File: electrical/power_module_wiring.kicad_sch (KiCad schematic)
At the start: 8 parts, among them J1 Power, J12 Conn_01x02_Pin, J13 11156, J14 Conn_01x02_Socket, J15 11155, J3 Bulb, J3 Ground

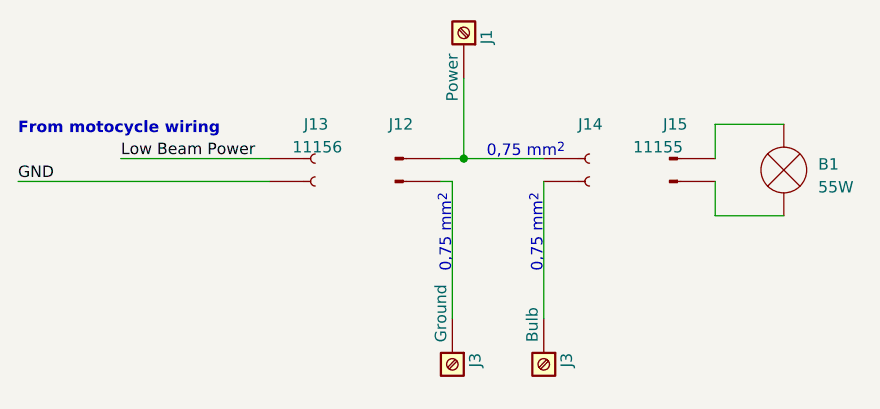
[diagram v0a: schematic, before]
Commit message: Electrical diagram refactor
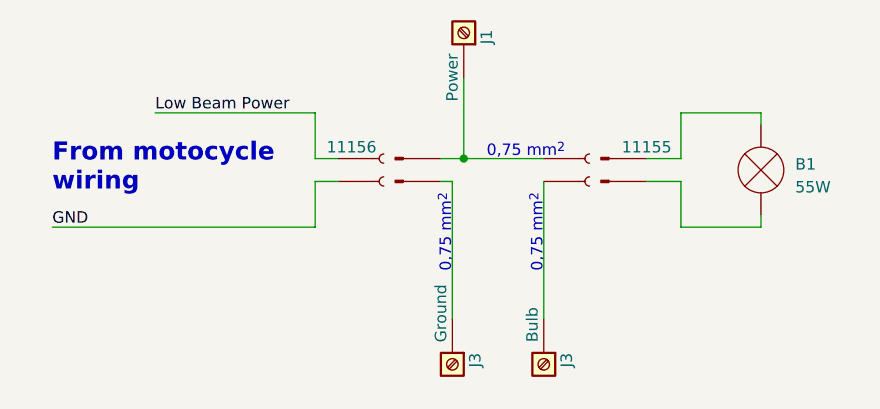
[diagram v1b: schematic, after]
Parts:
- renumbered J13 to J12, J12 to J13
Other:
- moved on the sheet: B1
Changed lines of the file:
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@@
   (junction (at 80.01 67.31) (diameter 0) (color 0 0 0 0)
   )
+  (wire (pts (xy 63.5 74.93) (xy 63.5 69.85))
+    (stroke (width 0) (type default))
+  )
+  (wire (pts (xy 113.03 74.93) (xy 113.03 73.66))
+    (stroke (width 0) (type default))
+  )
+  (wire (pts (xy 63.5 62.23) (xy 63.5 67.31))
+    (stroke (width 0) (type default))
+  )
   (wire (pts (xy 78.74 69.85) (xy 77.47 69.85))
     (stroke (width 0) (type default))
@@
     (stroke (width 0) (type default))
   )
-  (wire (pts (xy 41.91 67.31) (xy 58.42 67.31))
+  (wire (pts (xy 104.14 67.31) (xy 100.33 67.31))
+    (stroke (width 0) (type default))
+  )
+  (wire (pts (xy 45.72 62.23) (xy 63.5 62.23))
+    (stroke (width 0) (type default))
+  )
+  (wire (pts (xy 63.5 67.31) (xy 66.04 67.31))
     (stroke (width 0) (type default))
   )
@@
     (stroke (width 0) (type default))
   )
-  (wire (pts (xy 107.95 67.31) (xy 107.95 63.5))
-    (stroke (width 0) (type default))
-  )
-  (wire (pts (xy 107.95 63.5) (xy 115.57 63.5))
+  (wire (pts (xy 63.5 69.85) (xy 66.04 69.85))
+    (stroke (width 0) (type default))
+  )
+  (wire (pts (xy 113.03 62.23) (xy 113.03 63.5))
+    (stroke (width 0) (type default))
+  )
+  (wire (pts (xy 104.14 67.31) (xy 104.14 62.23))
+    (stroke (width 0) (type default))
+  )
+  (wire (pts (xy 104.14 62.23) (xy 113.03 62.23))
     (stroke (width 0) (type default))
   )
@@
     (stroke (width 0) (type default))
   )
-  (wire (pts (xy 30.48 69.85) (xy 58.42 69.85))
-    (stroke (width 0) (type default))
-  )
-  (wire (pts (xy 107.95 69.85) (xy 107.95 73.66))
-    (stroke (width 0) (type default))
-  )
-  (wire (pts (xy 107.95 73.66) (xy 115.57 73.66))
-    (stroke (width 0) (type default))
-  )
-  (text "From motocycle wiring" (at 30.48 64.77 0)
-    (effects (font (size 1.27 1.27) (thickness 0.254) bold) (justify left bottom))
+  (wire (pts (xy 104.14 69.85) (xy 100.33 69.85))
+    (stroke (width 0) (type default))
+  )
+  (wire (pts (xy 34.29 74.93) (xy 63.5 74.93))
+    (stroke (width 0) (type default))
+  )
+  (wire (pts (xy 104.14 69.85) (xy 104.14 74.93))
+    (stroke (width 0) (type default))
+  )
+  (wire (pts (xy 104.14 74.93) (xy 113.03 74.93))
+    (stroke (width 0) (type default))
+  )
+  (text "From motocycle\nwiring" (at 34.29 71.12 0)
+    (effects (font (size 2 2) (thickness 0.254) bold) (justify left bottom))
   )
   (text "0,75 mm^{2}" (at 82.55 67.31 0)
@@
     (effects (font (size 1.27 1.27)) (justify left bottom))
   )
-  (label "Low Beam Power" (at 41.91 67.31 0) (fields_autoplaced)
-    (effects (font (size 1.27 1.27)) (justify left bottom))
-    (property "Color" "B/Bl" (at 41.91 68.58 0) (show_name)
+  (label "Low Beam Power" (at 45.72 62.23 0) (fields_autoplaced)
+    (effects (font (size 1.27 1.27)) (justify left bottom))
+    (property "Color" "B/Bl" (at 45.72 63.5 0) (show_name)
       (effects (font (size 1.27 1.27) italic) (justify left))
     )
   )
-  (label "GND" (at 30.48 69.85 0) (fields_autoplaced)
-    (effects (font (size 1.27 1.27)) (justify left bottom))
-    (property "Color" "B/W" (at 30.48 71.12 0) (show_name)
+  (label "GND" (at 34.29 74.93 0) (fields_autoplaced)
+    (effects (font (size 1.27 1.27)) (justify left bottom))
+    (property "Color" "B/W" (at 34.29 76.2 0) (show_name)
       (effects (font (size 1.27 1.27) italic) (justify left))
     )
@@
     )
   )
-  (symbol (lib_name "Conn_01x02_Pin_1") (lib_id "Connector:Conn_01x02_Pin") (at 102.87 67.31 0) (unit 1)
-    (in_bom yes) (on_board yes) (dnp no)
-    (property "Reference" "J15" (at 103.505 63.5 0)
+  (symbol (lib_name "Conn_01x02_Pin_1") (lib_id "Connector:Conn_01x02_Pin") (at 95.25 67.31 0) (unit 1)
+    (in_bom yes) (on_board yes) (dnp no)
+    (property "Reference" "J15" (at 95.885 63.5 0)
+      (effects (font (size 1.27 1.27)) hide)
+    )
+    (property "Value" "11155" (at 100.33 66.04 0)
       (effects (font (size 1.27 1.27)))
     )
-    (property "Value" "11155" (at 101.6 66.04 0)
-      (effects (font (size 1.27 1.27)))
-    )
-    (property "Footprint" "" (at 102.87 67.31 0)
-      (effects (font (size 1.27 1.27)) hide)
-    )
-    (property "Datasheet" "~" (at 102.87 67.31 0)
+    (property "Footprint" "" (at 95.25 67.31 0)
+      (effects (font (size 1.27 1.27)) hide)
+    )
+    (property "Datasheet" "~" (at 95.25 67.31 0)
       (effects (font (size 1.27 1.27)) hide)
     )
@@
     )
   )
-  (symbol (lib_id "Connector:Conn_01x02_Socket") (at 63.5 67.31 0) (unit 1)
-    (in_bom yes) (on_board yes) (dnp no)
-    (property "Reference" "J13" (at 62.23 63.5 0)
-      (effects (font (size 1.27 1.27)) (justify left))
-    )
-    (property "Value" "11156" (at 60.96 66.04 0)
-      (effects (font (size 1.27 1.27)) (justify left))
-    )
-    (property "Footprint" "" (at 63.5 67.31 0)
-      (effects (font (size 1.27 1.27)) hide)
-    )
-    (property "Datasheet" "~" (at 63.5 67.31 0)
-      (effects (font (size 1.27 1.27)) hide)
-    )
-    (pin "1")
-    (pin "2")
-    (instances
-      (project "led_drive"
-        (path "/01e69042-7c7e-48e9-b7c3-459316fd17f1/0c65a6ac-9b7c-43de-8f27-03fd79afa39a"
-          (reference "J13") (unit 1)
-        )
-      )
-    )
-  )
-  (symbol (lib_id "Device:Lamp") (at 115.57 68.58 0) (unit 1)
+  (symbol (lib_id "Connector:Conn_01x02_Socket") (at 71.12 67.31 0) (unit 1)
+    (in_bom yes) (on_board yes) (dnp no)
+    (property "Reference" "J12" (at 69.85 63.5 0)
+      (effects (font (size 1.27 1.27)) (justify left) hide)
+    )
+    (property "Value" "11156" (at 64.77 66.04 0)
+      (effects (font (size 1.27 1.27)) (justify left))
+    )
+    (property "Footprint" "" (at 71.12 67.31 0)
+      (effects (font (size 1.27 1.27)) hide)
+    )
+    (property "Datasheet" "~" (at 71.12 67.31 0)
+      (effects (font (size 1.27 1.27)) hide)
+    )
+    (pin "1")
+    (pin "2")
+    (instances
+      (project "led_drive"
+        (path "/01e69042-7c7e-48e9-b7c3-459316fd17f1/0c65a6ac-9b7c-43de-8f27-03fd79afa39a"
+          (reference "J12") (unit 1)
+        )
+      )
+    )
+  )
+  (symbol (lib_id "Device:Lamp") (at 113.03 68.58 0) (unit 1)
     (in_bom no) (on_board no) (dnp no) (fields_autoplaced)
-    (property "Reference" "B1" (at 119.38 67.945 0)
-      (effects (font (size 1.27 1.27)) (justify left))
-    )
-    (property "Value" "55W" (at 119.38 70.485 0)
-      (effects (font (size 1.27 1.27)) (justify left))
-    )
-    (property "Footprint" "" (at 115.57 66.04 90)
-      (effects (font (size 1.27 1.27)) hide)
-    )
-    (property "Datasheet" "~" (at 115.57 66.04 90)
+    (property "Reference" "B1" (at 116.84 67.945 0)
+      (effects (font (size 1.27 1.27)) (justify left))
+    )
+    (property "Value" "55W" (at 116.84 70.485 0)
+      (effects (font (size 1.27 1.27)) (justify left))
+    )
+    (property "Footprint" "" (at 113.03 66.04 90)
+      (effects (font (size 1.27 1.27)) hide)
+    )
+    (property "Datasheet" "~" (at 113.03 66.04 90)
       (effects (font (size 1.27 1.27)) hide)
     )
@@
         )
         (path "/01e69042-7c7e-48e9-b7c3-459316fd17f1/0c65a6ac-9b7c-43de-8f27-03fd79afa39a"
-          (reference "B2") (unit 1)
+          (reference "B1") (unit 1)
         )
       )
@@
         )
         (path "/01e69042-7c7e-48e9-b7c3-459316fd17f1/0c65a6ac-9b7c-43de-8f27-03fd79afa39a"
-          (reference "J11") (unit 1)
+          (reference "J1") (unit 1)
         )
       )
@@
   (symbol (lib_name "Conn_01x02_Socket_1") (lib_id "Connector:Conn_01x02_Socket") (at 93.98 67.31 0) (unit 1)
     (in_bom yes) (on_board yes) (dnp no)
-    (property "Reference" "J14" (at 92.71 63.5 0)
-      (effects (font (size 1.27 1.27)) (justify left))
+    (property "Reference" "J14" (at 92.71 66.04 0)
+      (effects (font (size 1.27 1.27)) (justify left) hide)
     )
     (property "Value" "Conn_01x02_Socket" (at 95.25 70.485 0)
@@
   (symbol (lib_id "Connector:Conn_01x02_Pin") (at 72.39 67.31 0) (unit 1)
     (in_bom yes) (on_board yes) (dnp no) (fields_autoplaced)
-    (property "Reference" "J12" (at 73.025 63.5 0)
-      (effects (font (size 1.27 1.27)))
+    (property "Reference" "J13" (at 73.025 66.04 0)
+      (effects (font (size 1.27 1.27)) hide)
     )
     (property "Value" "Conn_01x02_Pin" (at 73.025 66.04 0)
@@
       (project "led_drive"
         (path "/01e69042-7c7e-48e9-b7c3-459316fd17f1/0c65a6ac-9b7c-43de-8f27-03fd79afa39a"
-          (reference "J12") (unit 1)
-        )
-      )
+          (reference "J13") (unit 1)
+        )
+      )

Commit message: electrical module draft
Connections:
- net Low Beam Power renamed LO Beam Power
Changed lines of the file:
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@@
     (effects (font (size 1.27 1.27)) (justify left bottom))
   )
-  (label "Low Beam Power" (at 45.72 62.23 0) (fields_autoplaced)
+  (label "LO Beam Power" (at 45.72 62.23 0) (fields_autoplaced)
     (effects (font (size 1.27 1.27)) (justify left bottom))
     (property "Color" "B/Bl" (at 45.72 63.5 0) (show_name)
@@
         (path "/01e69042-7c7e-48e9-b7c3-459316fd17f1"
           (reference "J1") (unit 1)
-        )
-        (path "/01e69042-7c7e-48e9-b7c3-459316fd17f1/bc381f99-814a-407f-b047-30e2660febd1"
-          (reference "J3") (unit 1)
         )
         (path "/01e69042-7c7e-48e9-b7c3-459316fd17f1/8dbccfbf-0961-4856-9879-280cfe95837a"
@@
     (instances
       (project "led_drive"
-        (path "/01e69042-7c7e-48e9-b7c3-459316fd17f1/bc381f99-814a-407f-b047-30e2660febd1"
-          (reference "B1") (unit 1)
-        )
         (path "/01e69042-7c7e-48e9-b7c3-459316fd17f1/8dbccfbf-0961-4856-9879-280cfe95837a"
           (reference "B2") (unit 1)
@@
         (path "/01e69042-7c7e-48e9-b7c3-459316fd17f1"
           (reference "J3") (unit 1)
-        )
-        (path "/01e69042-7c7e-48e9-b7c3-459316fd17f1/bc381f99-814a-407f-b047-30e2660febd1"
-          (reference "J2") (unit 1)
         )
         (path "/01e69042-7c7e-48e9-b7c3-459316fd17f1/8dbccfbf-0961-4856-9879-280cfe95837a"
@@
           (reference "J3") (unit 1)
         )
-        (path "/01e69042-7c7e-48e9-b7c3-459316fd17f1/bc381f99-814a-407f-b047-30e2660febd1"
-          (reference "J2") (unit 1)
-        )
         (path "/01e69042-7c7e-48e9-b7c3-459316fd17f1/8dbccfbf-0961-4856-9879-280cfe95837a"

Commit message: Work in progress
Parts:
- renumbered B1 to B2
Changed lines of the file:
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@@
   (symbol (lib_id "Device:Lamp") (at 113.03 68.58 0) (unit 1)
     (in_bom no) (on_board no) (dnp no) (fields_autoplaced)
-    (property "Reference" "B1" (at 116.84 67.945 0)
+    (property "Reference" "B2" (at 116.84 67.945 0)
       (effects (font (size 1.27 1.27)) (justify left))
     )

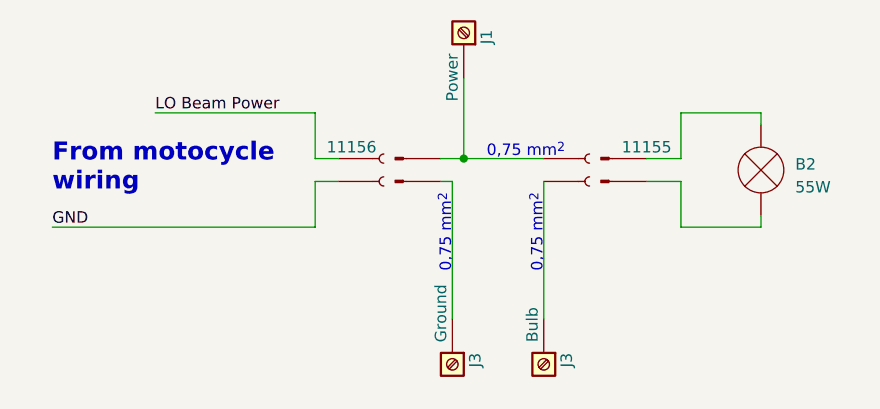
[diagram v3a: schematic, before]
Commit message: Name refactor
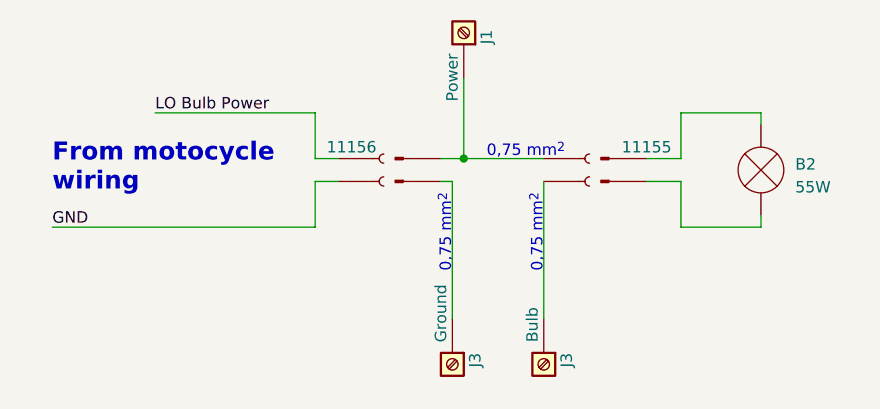
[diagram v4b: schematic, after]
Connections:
- net LO Beam Power renamed LO Bulb Power
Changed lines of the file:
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@@
     (effects (font (size 1.27 1.27)) (justify left bottom))
   )
-  (label "LO Beam Power" (at 45.72 62.23 0) (fields_autoplaced)
+  (label "LO Bulb Power" (at 45.72 62.23 0) (fields_autoplaced)
     (effects (font (size 1.27 1.27)) (justify left bottom))
     (property "Color" "B/Bl" (at 45.72 63.5 0) (show_name)

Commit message: Aktualizacja KiCad i schematu - LED do debugowania
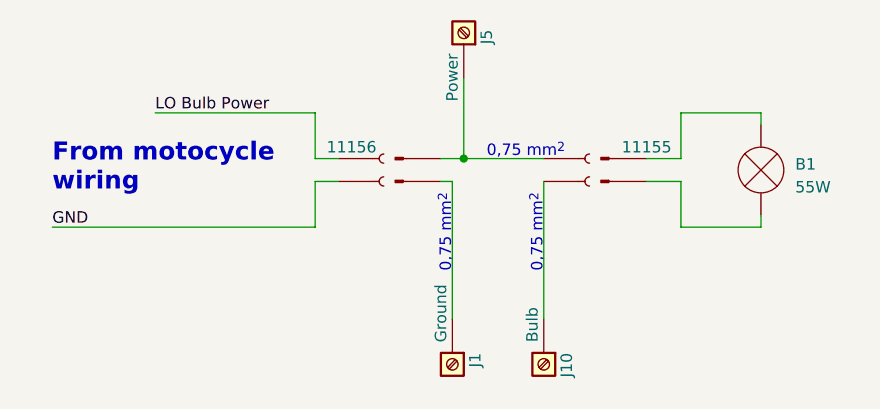
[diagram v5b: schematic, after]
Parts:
- renumbered B2 to B1, J3 to J1, J3 to J10, J1 to J5
